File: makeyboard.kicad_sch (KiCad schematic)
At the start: 0 parts

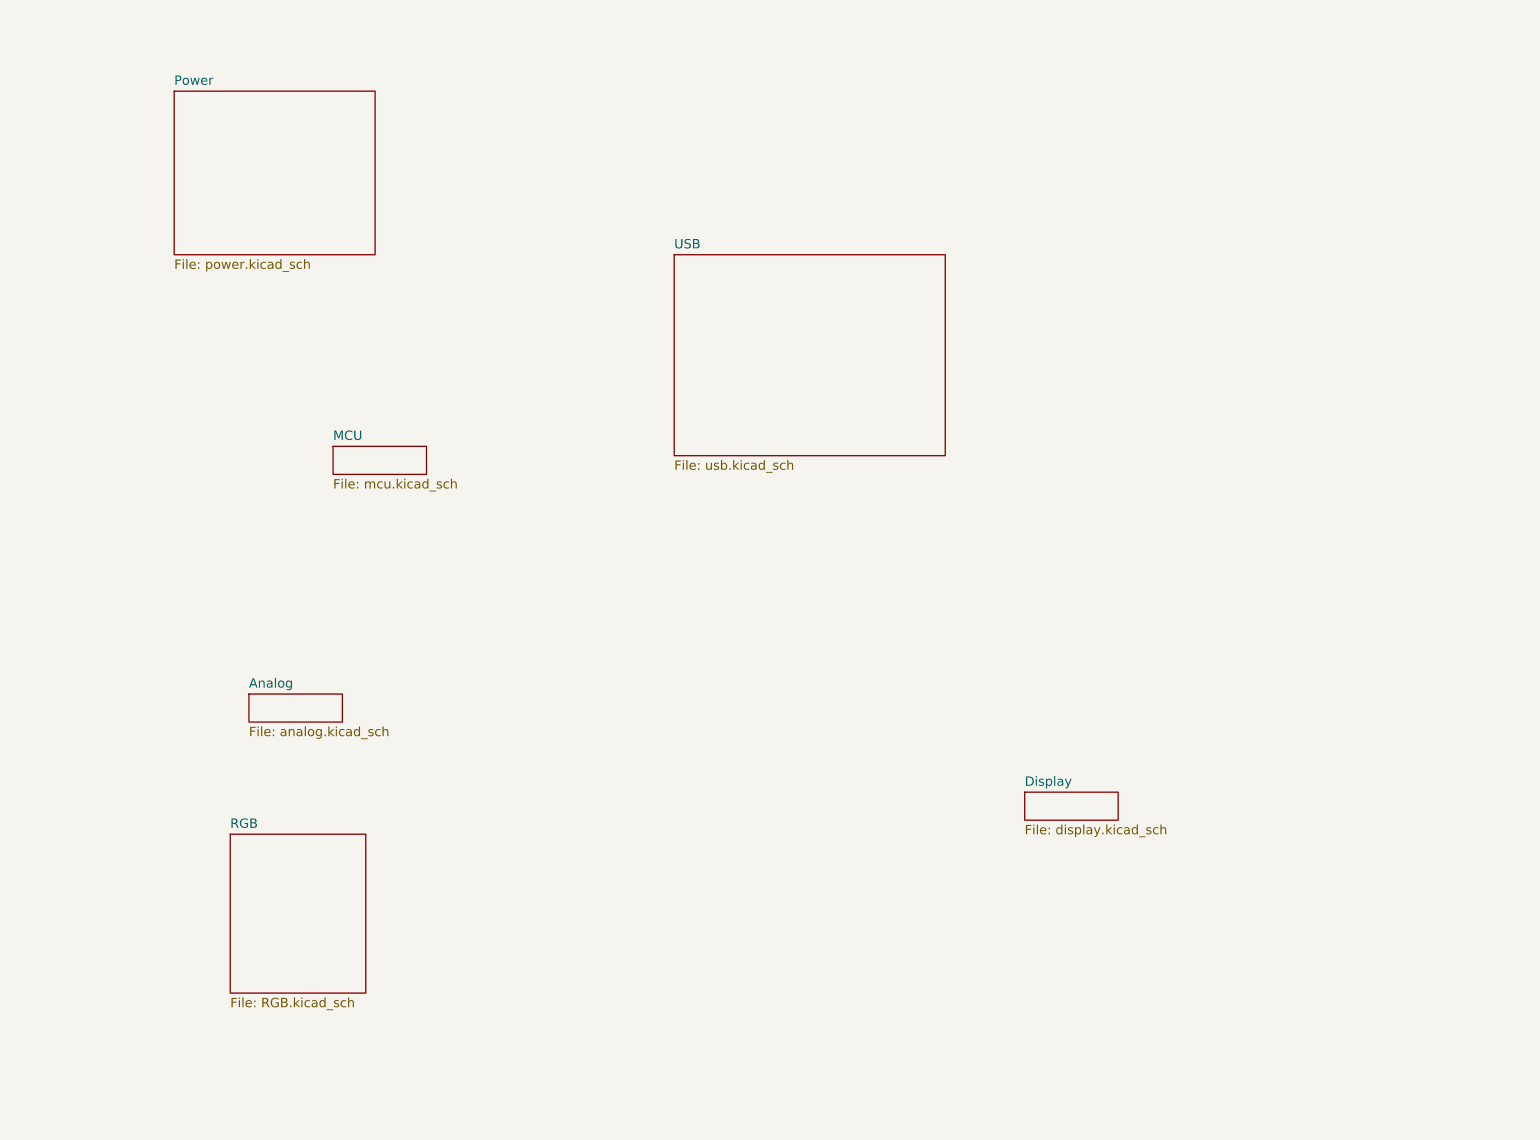
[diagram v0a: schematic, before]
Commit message: add decoupling pins
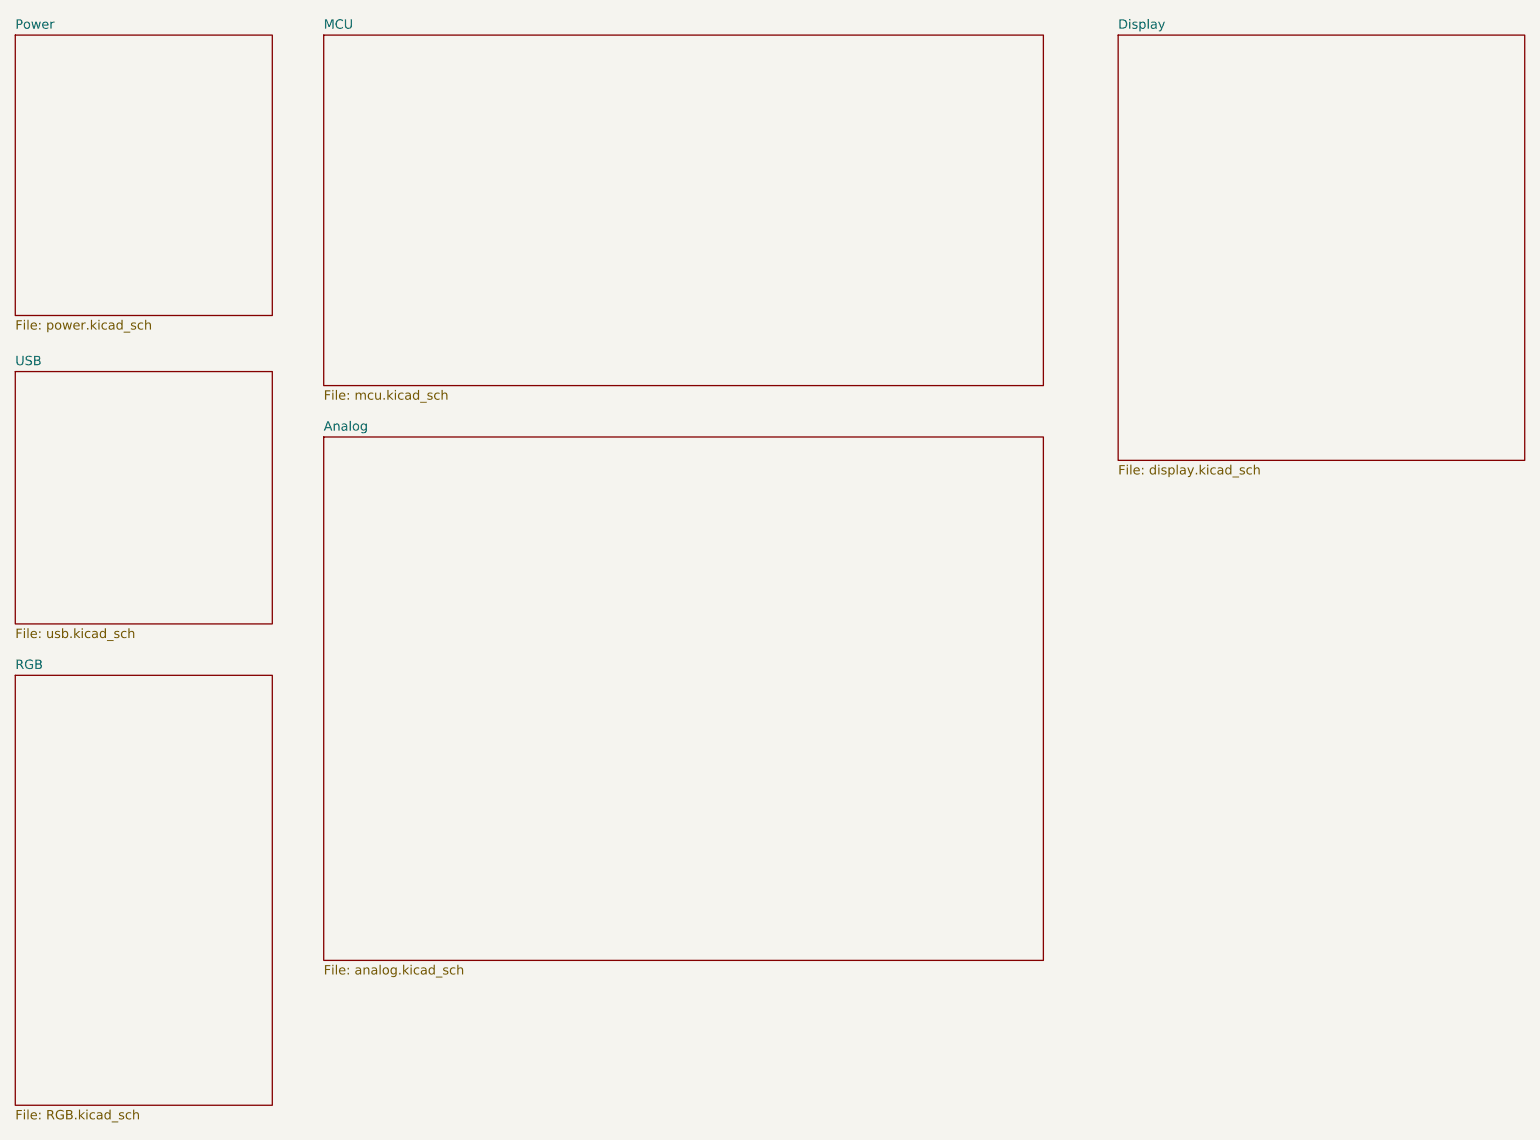
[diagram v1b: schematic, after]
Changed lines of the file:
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@@
 	(paper "A4")
 	(sheet
-		(at 69.215 80.645)
-		(size 12.7 3.81)
+		(at 67.945 24.765)
+		(size 97.79 47.625)
 		(exclude_from_sim no)
 		(in_bom yes)
@@
 		)
 		(property "Sheetname" "MCU"
-			(at 69.215 79.9334 0)
+			(at 67.945 24.0534 0)
 			(show_name no)
 			(do_not_autoplace no)
@@
 		)
 		(property "Sheetfile" "mcu.kicad_sch"
-			(at 69.215 85.0396 0)
+			(at 67.945 72.9746 0)
 			(show_name no)
 			(do_not_autoplace no)
@@
 	)
 	(sheet
-		(at 115.57 54.61)
-		(size 36.83 27.305)
+		(at 26.035 70.485)
+		(size 34.925 34.29)
 		(exclude_from_sim no)
 		(in_bom yes)
@@
 		)
 		(property "Sheetname" "USB"
-			(at 115.57 53.8984 0)
+			(at 26.035 69.7734 0)
 			(show_name no)
 			(do_not_autoplace no)
@@
 		)
 		(property "Sheetfile" "usb.kicad_sch"
-			(at 115.57 82.4996 0)
+			(at 26.035 105.3596 0)
 			(show_name no)
 			(do_not_autoplace no)
@@
 	)
 	(sheet
-		(at 55.245 133.35)
-		(size 18.415 21.59)
+		(at 26.035 111.76)
+		(size 34.925 58.42)
 		(exclude_from_sim no)
 		(in_bom yes)
@@
 		)
 		(property "Sheetname" "RGB"
-			(at 55.245 132.6384 0)
+			(at 26.035 111.0484 0)
 			(show_name no)
 			(do_not_autoplace no)
@@
 		)
 		(property "Sheetfile" "RGB.kicad_sch"
-			(at 55.245 155.5246 0)
+			(at 26.035 170.7646 0)
 			(show_name no)
 			(do_not_autoplace no)
@@
 	)
 	(sheet
-		(at 57.785 114.3)
-		(size 12.7 3.81)
+		(at 67.945 79.375)
+		(size 97.79 71.12)
 		(exclude_from_sim no)
 		(in_bom yes)
@@
 		)
 		(property "Sheetname" "Analog"
-			(at 57.785 113.5884 0)
+			(at 67.945 78.6634 0)
 			(show_name no)
 			(do_not_autoplace no)
@@
 		)
 		(property "Sheetfile" "analog.kicad_sch"
-			(at 57.785 118.6946 0)
+			(at 67.945 151.0796 0)
 			(show_name no)
 			(do_not_autoplace no)
@@
 	)
 	(sheet
-		(at 163.195 127.635)
-		(size 12.7 3.81)
+		(at 175.895 24.765)
+		(size 55.245 57.785)
 		(exclude_from_sim no)
 		(in_bom yes)
@@
 		)
 		(property "Sheetname" "Display"
-			(at 163.195 126.9234 0)
+			(at 175.895 24.0534 0)
 			(show_name no)
 			(do_not_autoplace no)
@@
 		)
 		(property "Sheetfile" "display.kicad_sch"
-			(at 163.195 132.0296 0)
+			(at 175.895 83.1346 0)
 			(show_name no)
 			(do_not_autoplace no)
@@
 	)
 	(sheet
-		(at 47.625 32.385)
-		(size 27.305 22.225)
+		(at 26.035 24.765)
+		(size 34.925 38.1)
 		(exclude_from_sim no)
 		(in_bom yes)
@@
 		)
 		(property "Sheetname" "Power"
-			(at 47.625 31.6734 0)
+			(at 26.035 24.0534 0)
 			(show_name no)
 			(do_not_autoplace no)
@@
 		)
 		(property "Sheetfile" "power.kicad_sch"
-			(at 47.625 55.1946 0)
-			(show_name no)
-			(do_not_autoplace no)
+			(at 26.035 63.4496 0)
+			(show_name no)
+			(do_not_autoplace no)

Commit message: add sensors and muxes
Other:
- sheet RGB: file RGB.kicad_sch -> rgb.kicad_sch
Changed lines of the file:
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@@
 			)
 		)
-		(property "Sheetfile" "RGB.kicad_sch"
+		(property "Sheetfile" "rgb.kicad_sch"
 			(at 26.035 170.7646 0)
 			(show_name no)
